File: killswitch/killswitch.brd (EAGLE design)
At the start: 42.3 x 42.3 mm, 32 parts, among them U1 CD4012BPWR, U2 2N7002-7-F

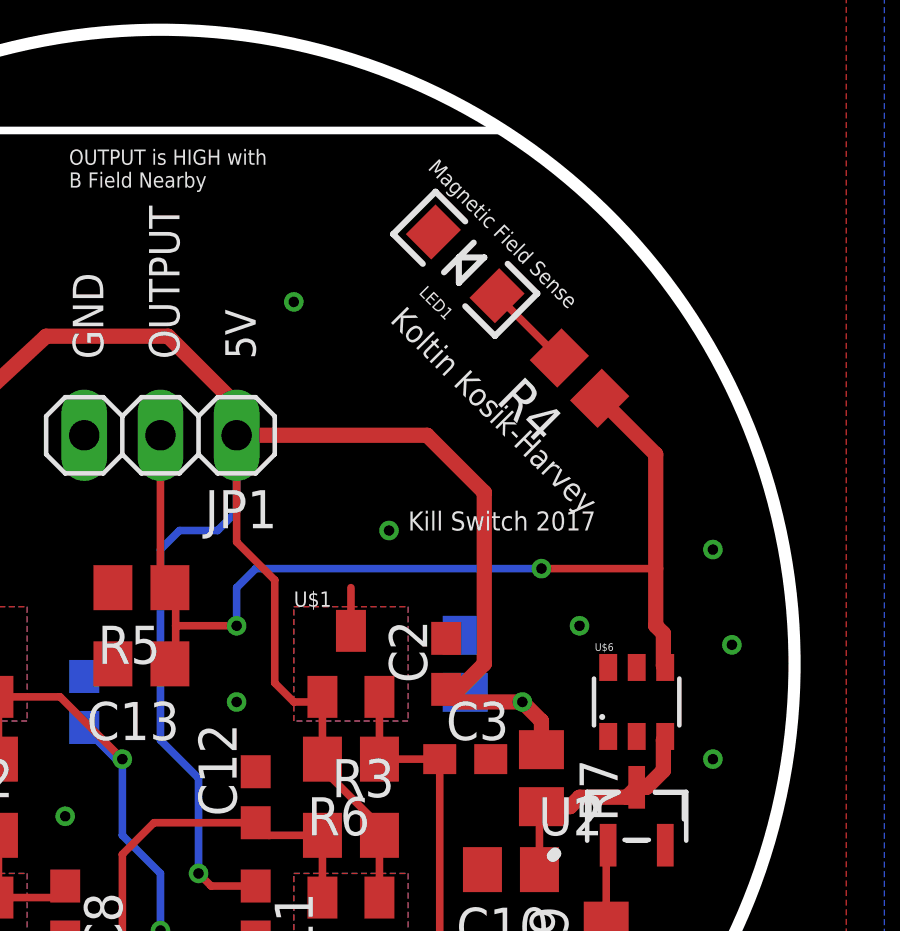
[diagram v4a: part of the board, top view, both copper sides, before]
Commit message: pMOS in schematic wasn't attached to 5V. Fixed that.
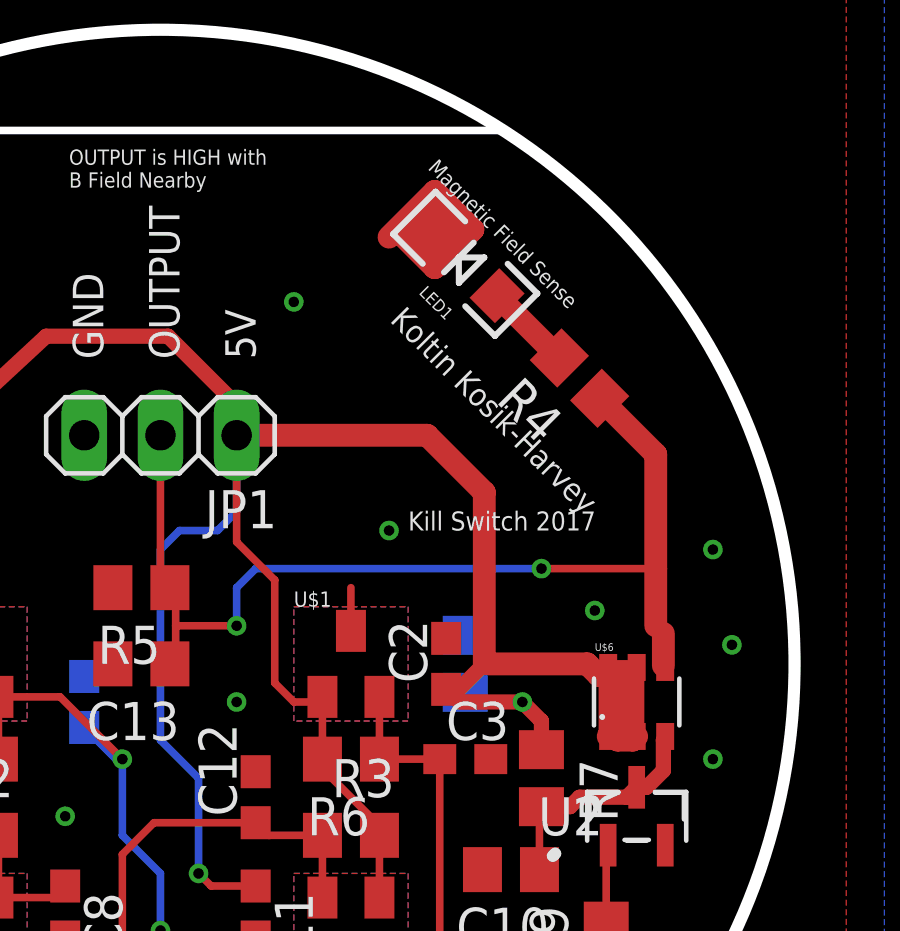
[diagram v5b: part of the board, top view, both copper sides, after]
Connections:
- net +5V: now also U$6.DRAIN, U$6.DRAIN2, U$6.DRAIN3, U$6.DRAIN4
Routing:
- net +5V: track 134.1 -> 148.8 mm
- net GND: track 5.76 -> 12.9 mm
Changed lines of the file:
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@@
 <via x="38.735" y="14.605" extent="1-16" drill="0.35"/>
 <via x="39.37" y="18.415" extent="1-16" drill="0.35"/>
-<via x="34.29" y="19.05" extent="1-16" drill="0.35"/>
+<via x="34.798" y="19.558" extent="1-16" drill="0.35"/>
 <wire x1="26.67" y1="18.88" x2="26.67" y2="20.32" width="0.254" layer="1"/>
 <contactref element="C7" pad="2"/>
@@
 <contactref element="C10" pad="2"/>
 <contactref element="JP1" pad="3"/>
+<wire x1="27.94" y1="32.004" x2="29.464" y2="33.528" width="0.762" layer="1"/>
+<wire x1="29.464" y1="33.528" x2="30.734" y2="32.258" width="0.762" layer="1"/>
+<wire x1="30.734" y1="32.258" x2="29.464" y2="30.988" width="0.762" layer="1"/>
+<wire x1="29.464" y1="30.988" x2="28.448" y2="32.004" width="0.762" layer="1"/>
 </signal>
 <signal name="+5V">
@@
 <wire x1="30.055" y1="16.72" x2="30.265" y2="16.51" width="0.254" layer="1"/>
 <wire x1="30.055" y1="16.72" x2="29.845" y2="16.93" width="0.254" layer="1"/>
-<wire x1="31.115" y1="17.78" x2="31.115" y2="23.495" width="0.508" layer="1"/>
+<wire x1="31.115" y1="17.78" x2="31.115" y2="23.495" width="0.762" layer="1"/>
 <wire x1="31.115" y1="17.78" x2="30.055" y2="16.72" width="0.508" layer="1"/>
 <contactref element="C7" pad="1"/>
@@
 <wire x1="22.86" y1="25.4" x2="22.606" y2="25.654" width="0.508" layer="1"/>
 <wire x1="20.574" y1="28.702" x2="22.606" y2="26.67" width="0.508" layer="1"/>
-<wire x1="31.115" y1="23.495" x2="29.21" y2="25.4" width="0.508" layer="1"/>
-<wire x1="29.21" y1="25.4" x2="22.86" y2="25.4" width="0.508" layer="1"/>
+<wire x1="31.115" y1="23.495" x2="29.21" y2="25.4" width="0.762" layer="1"/>
+<wire x1="29.21" y1="25.4" x2="22.86" y2="25.4" width="0.762" layer="1"/>
 <wire x1="24.13" y1="20.574" x2="22.86" y2="21.844" width="0.254" layer="1"/>
 <wire x1="22.86" y1="21.844" x2="22.86" y2="25.4" width="0.254" layer="1"/>
 <wire x1="24.13" y1="17.145" x2="24.13" y2="20.574" width="0.254" layer="1"/>
+<contactref element="U$6" pad="DRAIN"/>
+<contactref element="U$6" pad="DRAIN2"/>
+<contactref element="U$6" pad="DRAIN4"/>
+<contactref element="U$6" pad="DRAIN3"/>
+<wire x1="36.195" y1="15.36" x2="35.245" y2="15.36" width="0.762" layer="1"/>
+<wire x1="35.245" y1="17.66" x2="36.195" y2="17.66" width="0.254" layer="1"/>
+<wire x1="36.195" y1="17.66" x2="36.195" y2="15.36" width="0.254" layer="1"/>
+<wire x1="31.242" y1="17.78" x2="34.544" y2="17.78" width="0.762" layer="1"/>
+<wire x1="34.925" y1="17.399" x2="34.544" y2="17.78" width="0.762" layer="1"/>
+<wire x1="35.306" y1="17.018" x2="35.306" y2="15.494" width="0.762" layer="1"/>
+<wire x1="35.306" y1="15.494" x2="35.56" y2="15.24" width="0.762" layer="1"/>
+<wire x1="35.56" y1="15.24" x2="36.068" y2="15.24" width="0.762" layer="1"/>
+<wire x1="36.068" y1="15.24" x2="36.068" y2="17.526" width="0.762" layer="1"/>
+<wire x1="36.068" y1="17.526" x2="35.052" y2="17.526" width="0.762" layer="1"/>
+<wire x1="35.052" y1="17.526" x2="34.925" y2="17.399" width="0.762" layer="1"/>
+<wire x1="35.56" y1="16.51" x2="35.814" y2="17.272" width="0.254" layer="1"/>
+<wire x1="36.068" y1="17.526" x2="35.814" y2="17.272" width="0" layer="19" extent="1-1"/>
+<wire x1="31.115" y1="17.78" x2="31.242" y2="17.78" width="0" layer="19" extent="1-1"/>
+<wire x1="35.245" y1="15.36" x2="35.306" y2="15.494" width="0" layer="19" extent="1-1"/>
 </signal>
 <signal name="N$5">
@@
 <via x="22.86" y="19.05" extent="1-16" drill="0.35"/>
 <contactref element="R4" pad="1"/>
-<wire x1="36.83" y1="24.764996875" x2="34.96175" y2="26.633246875" width="0.508" layer="1"/>
-<wire x1="36.83" y1="20.955" x2="36.83" y2="24.764996875" width="0.508" layer="1"/>
+<wire x1="36.83" y1="24.764996875" x2="34.96175" y2="26.633246875" width="0.762" layer="1"/>
+<wire x1="36.83" y1="20.955" x2="36.83" y2="24.764996875" width="0.762" layer="1"/>
 <contactref element="U$6" pad="SOURCE"/>
 <contactref element="R5" pad="1"/>
 <contactref element="C13" pad="1"/>
-<wire x1="36.83" y1="20.955" x2="36.83" y2="19.05" width="0.508" layer="1"/>
+<wire x1="36.83" y1="20.955" x2="36.83" y2="19.05" width="0.762" layer="1"/>
 <wire x1="36.83" y1="19.05" x2="37.084" y2="18.796" width="0.508" layer="1"/>
-<wire x1="37.084" y1="18.796" x2="37.084" y2="17.721" width="0.508" layer="1"/>
+<wire x1="37.084" y1="18.796" x2="37.084" y2="17.721" width="0.762" layer="1"/>
 <wire x1="37.084" y1="17.721" x2="37.145" y2="17.66" width="0.508" layer="1"/>
 <wire x1="20.828" y1="20.127" x2="20.828" y2="19.05" width="0.254" layer="1"/>
@@
 <contactref element="R4" pad="2"/>
 <contactref element="LED1" pad="A"/>
-<wire x1="33.618246875" y1="27.97675" x2="31.540659375" y2="30.0543375" width="0.254" layer="1"/>
+<wire x1="33.618246875" y1="27.97675" x2="31.540659375" y2="30.0543375" width="0.762" layer="1"/>
 </signal>
 <signal name="N$9">

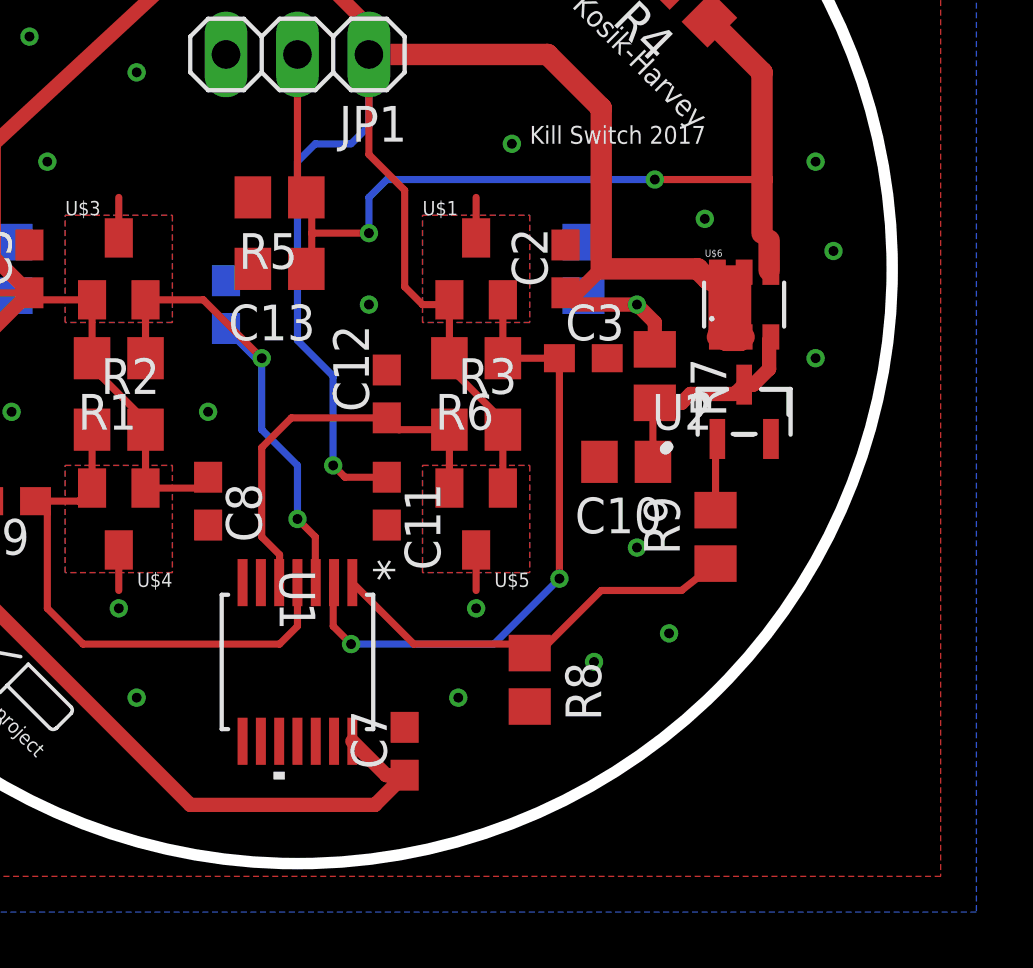
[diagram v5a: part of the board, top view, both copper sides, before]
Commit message: Output wasnt pulling low. Using a push-pull buffer and an AND gate instead
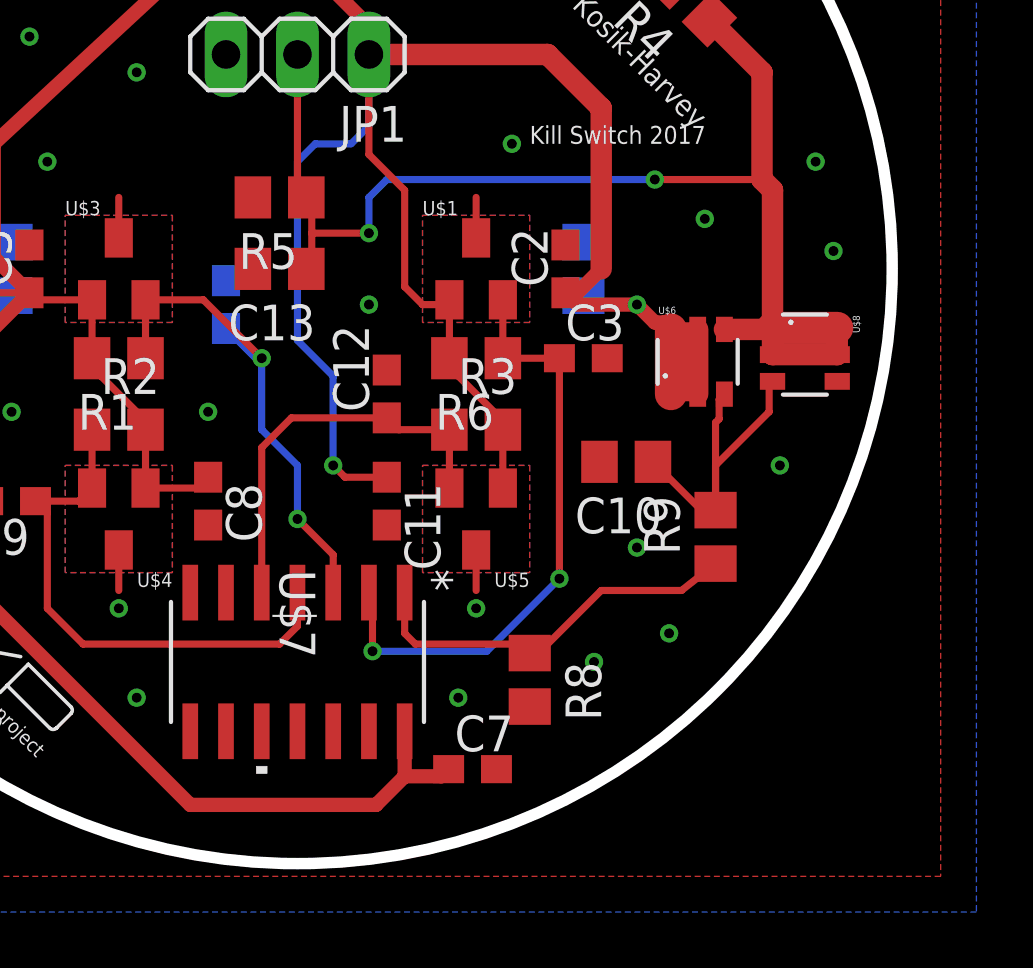
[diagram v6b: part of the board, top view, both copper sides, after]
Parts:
- removed R7: 10k, resistor:R0805
- removed U1: CD4012BPWR, KillSwitch:PW14
- removed U2: 2N7002-7-F, KillSwitch:SOT-23
- added U$7: CD4082BM96, KillSwitch:D14
- added U$8: IRLMS2002TRPBF, KillSwitch:SOT23-6
- moved U$6 2.62 mm to (34.5, 14.5)
- moved C7 2.50 mm to (26.5, 0.00), turned to 0 degrees
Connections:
- removed net N$9: C10.1, R7.2, U$6.GATE, U2.3
- removed net NAND_OUTPUT: R8.1, R9.1, U1.1
- new net AND_OUTPUT: R8.1, R9.1, U$7.1
- net +5V: now also U$7.14; no longer R7.1, U1.14
- net GND: now also U$7.10, U$7.11, U$7.12, U$7.6, U$7.7, U$7.8, U$7.9, U$8.SOURCE; no longer U1.10, U1.11, U1.12, U1.6, U1.7, U1.8, U1.9, U2.2
- net N$1: now also U$7.3; no longer U1.3
- net N$10: now also C10.1, U$6.GATE, U$8.GATE; no longer U2.1
- net N$2: now also U$7.4; no longer U1.4
- net N$3: now also U$7.5; no longer U1.5
- net N$5: now also U$7.2; no longer U1.2
- net OUTPUT: now also U$8.DRAIN, U$8.DRAIN2, U$8.DRAIN3, U$8.DRAIN4
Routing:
- net NAND_OUTPUT: track 15.7 -> 0.00 mm
- net AND_OUTPUT: track 0.00 -> 14.5 mm
- net N$10: track 2.54 -> 13.0 mm
- net OUTPUT: track 35.8 -> 46.0 mm
- net N$9: track 7.85 -> 0.00 mm
- net +5V: track 148.8 -> 141.2 mm
- net N$5: track 22.7 -> 21.8 mm
- net N$1: track 17.5 -> 18.2 mm

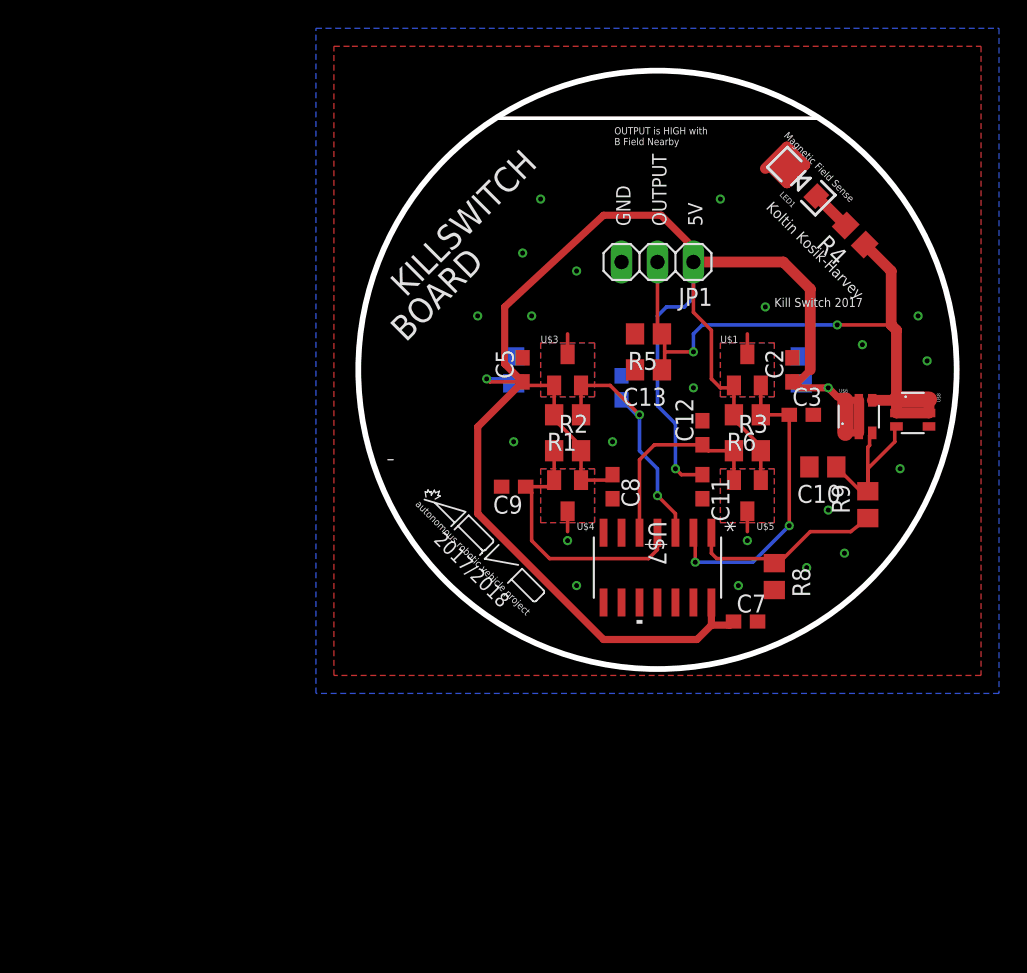
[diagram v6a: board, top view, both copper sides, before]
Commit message: AND gate turned out to be redundant. Removed it.
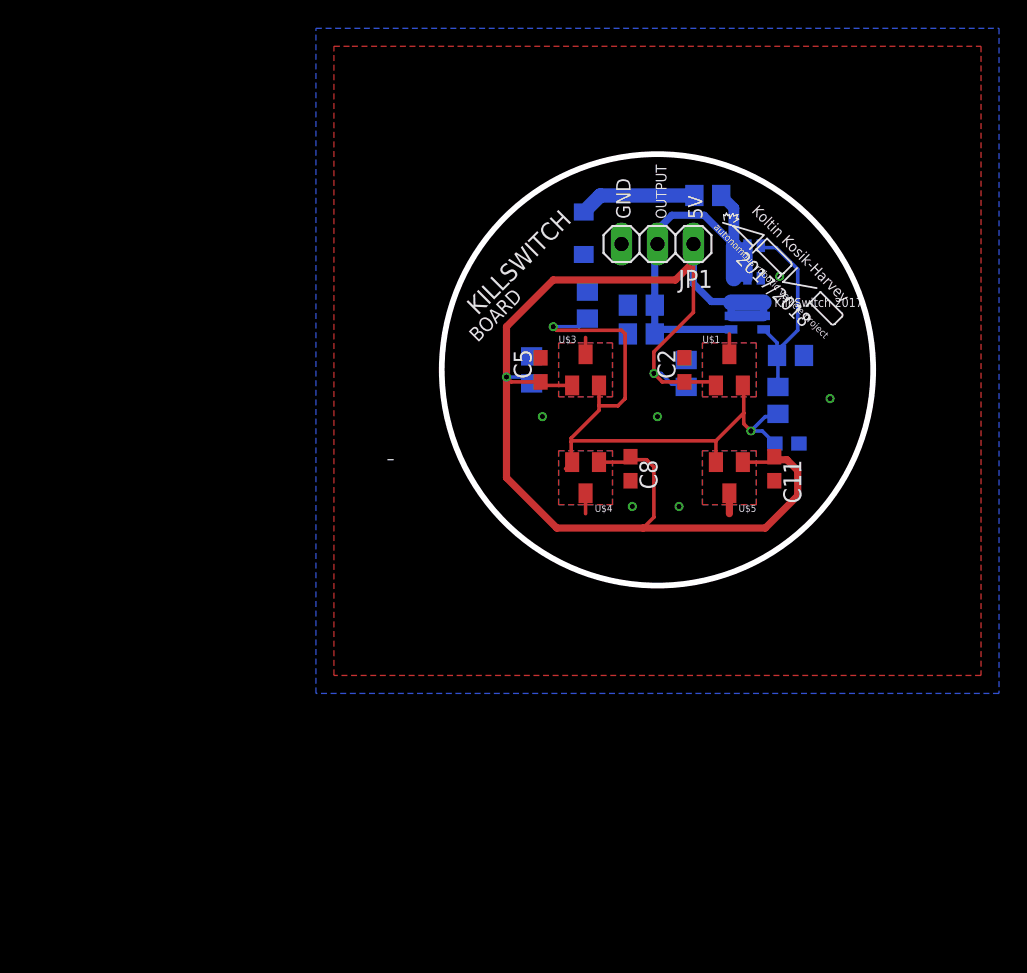
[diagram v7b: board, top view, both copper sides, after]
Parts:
- removed C12, C6, C7, C9: 1uF, resistor:C0603
- removed R1, R2, R3, R8: 10k, resistor:R0805
- removed U$7: CD4082BM96, KillSwitch:D14
- moved U$2 28.8 mm to (24.3, 27.8)
- moved U$8 15.8 mm to (26.7, 25.4), flipped to the bottom, turned to 180 degrees
- moved LED1 15.8 mm to (15.1, 27.4), flipped to the bottom, turned to 270 degrees
- moved R6 13.7 mm to (15.4, 22.4), flipped to the bottom, turned to 90 degrees
- moved R4 10.8 mm to (23.9, 30.1), flipped to the bottom, turned to 0 degrees
- moved U$6 10.6 mm to (26.7, 21.6), flipped to the bottom, turned to 270 degrees
- moved R9 9.73 mm to (28.8, 15.6), flipped to the bottom
- moved C10 8.20 mm to (29.7, 18.8), flipped to the bottom
- moved C1 8.13 mm to (22.4, 17.5)
- moved C2 7.62 mm to (22.2, 17.8)
- moved C11 5.24 mm to (28.6, 10.8)
- moved C13 2.59 mm to (19.2, 20.3), flipped to the bottom, turned to 0 degrees
- moved C3 2.27 mm to (29.5, 12.6), flipped to the bottom, turned to 180 degrees
- moved R5 2.09 mm to (19.2, 22.4), flipped to the bottom, turned to 0 degrees
- moved U$5 1.80 mm to (25.4, 10.2)
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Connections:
- removed net AND_OUTPUT: R8.1, R9.1, U$7.1
- removed net N$1: C6.1, R1.1, U$3.OUTPUT, U$7.3
- removed net N$2: C9.1, R2.1, U$4.OUTPUT, U$7.4
- removed net N$3: C12.1, R3.1, U$5.OUTPUT, U$7.5
- net +5V: no longer C7.1, R1.2, R2.2, R3.2, U$7.14
- net GND: no longer C12.2, C6.2, C7.2, C9.2, R8.2, U$7.10, U$7.11, U$7.12, U$7.6, U$7.7, U$7.8, U$7.9
- net N$5: now also R9.1, U$3.OUTPUT, U$4.OUTPUT, U$5.OUTPUT; no longer U$7.2
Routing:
- net +5V: track 141.2 -> 102.5 mm, vias 3 -> 2
- net N$5: track 21.8 -> 43.9 mm
- net N$2: track 19.1 -> 0.00 mm
- net N$1: track 18.2 -> 0.00 mm, vias 2 -> 0
- net OUTPUT: track 46.0 -> 30.4 mm, vias 2 -> 0
- net AND_OUTPUT: track 14.5 -> 0.00 mm
- net N$3: track 14.5 -> 0.00 mm
- net GND: track 12.9 -> 5.51 mm, vias 21 -> 6
- net N$8: track 2.94 -> 8.30 mm
- net N$10: track 13.0 -> 14.5 mm
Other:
- board size 42.3 x 42.3 mm -> 30.5 x 30.5 mm
